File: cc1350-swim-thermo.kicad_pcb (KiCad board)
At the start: 4 copper layers, 60.9 x 60.9 mm, 54 parts, among them P1 LMT_70_1, P2 LMT_70_2, P3 SMA FEMALE, P4 USB_OTG, P5 CONN_02X05, Q1 2N7002, SW1 SW_Push, U1 2450BM14G0011T, U2 XMSSJE3G0PA-003, U3 CC1350F128RSM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

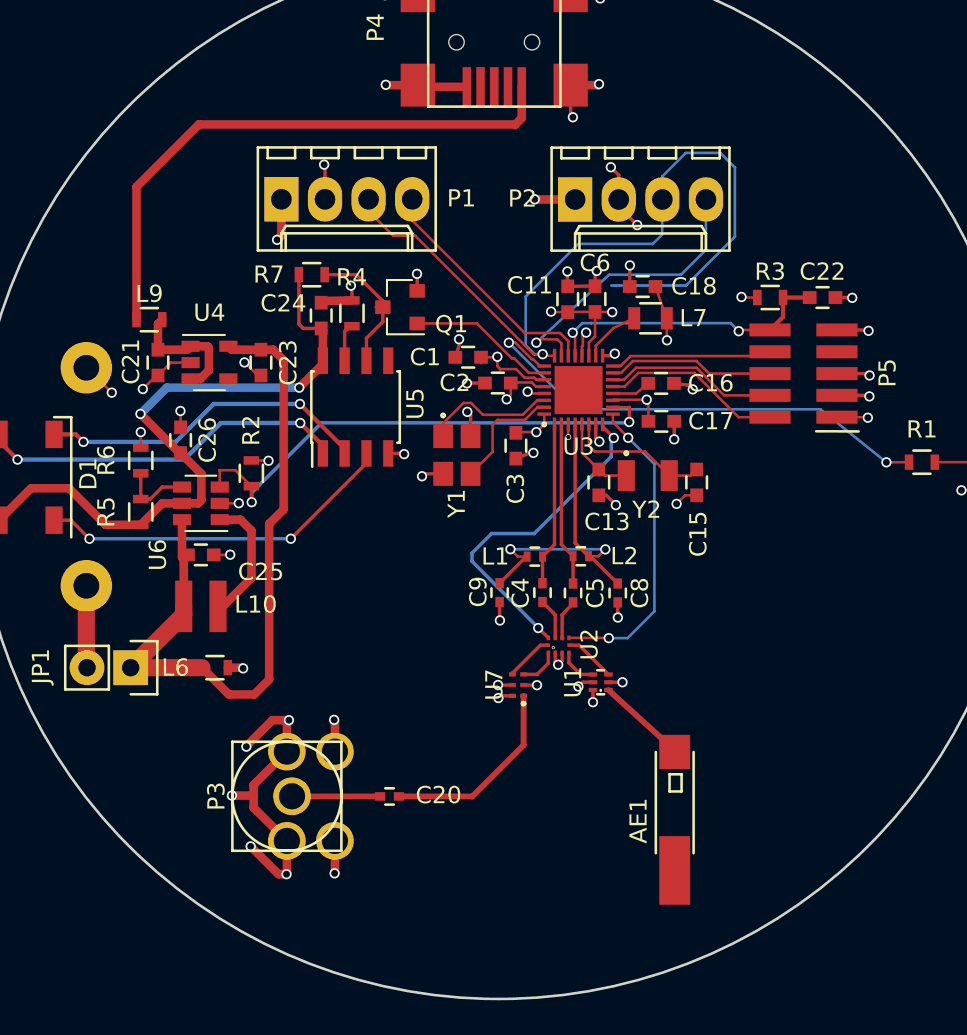
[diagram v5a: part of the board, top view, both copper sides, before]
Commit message: finished wiring, labels and mounting holes
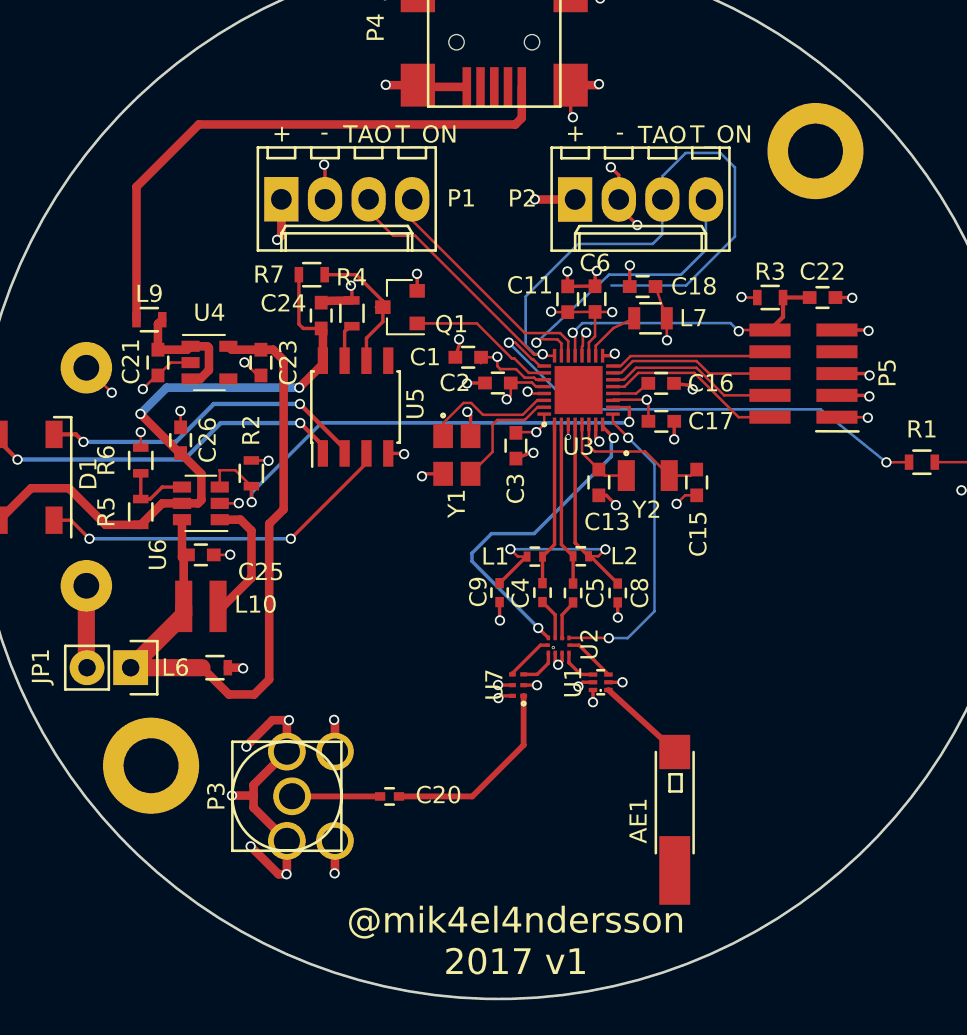
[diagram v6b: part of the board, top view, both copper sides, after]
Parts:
- added REF**: MountingHole_3.2mm_M3_DIN965_Pad, Mounting_Holes:MountingHole_3.2mm_M3_DIN965_Pad, F.Cu at (128.4, 89.3)
- added REF**: MountingHole_3.2mm_M3_DIN965_Pad, Mounting_Holes:MountingHole_3.2mm_M3_DIN965_Pad, F.Cu at (89.7, 125.1)
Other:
- board text added: "+"
- board text added: "-"
- board text added: "@mik4el4ndersson 2017 v1"
- board text added: "Sensor node/concentrator CC1350 sub-GHz and BLE USB or 2xAAA battery"
- board text added: "TAO"
- board text added: "T_ON"

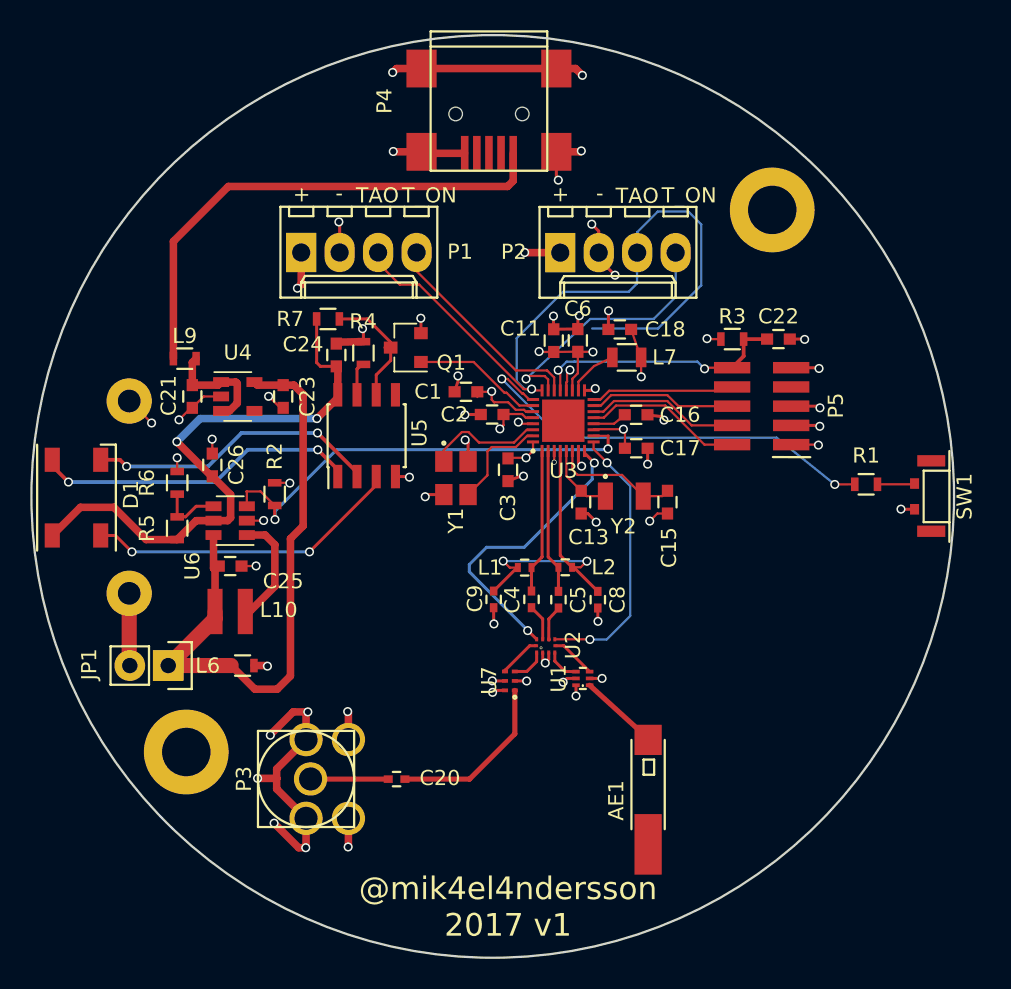
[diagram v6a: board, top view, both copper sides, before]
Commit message: checked first iteration of pcb with real components
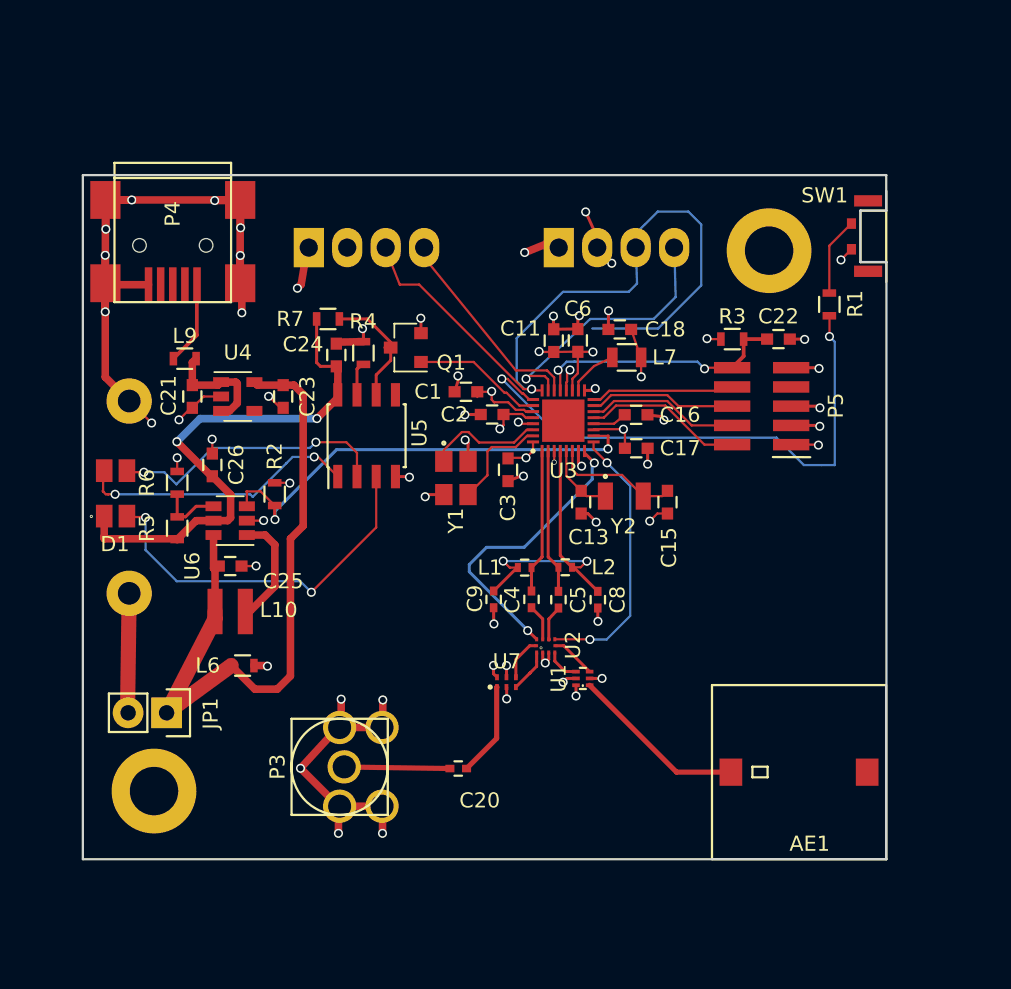
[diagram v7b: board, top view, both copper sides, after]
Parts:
- removed the REF** at (128.4, 89.3)
- removed the REF** at (89.7, 125.1)
- added REF**: MountingHole_3.2mm_M3_DIN965_Pad, Mounting_Holes:MountingHole_3.2mm_M3_DIN965_Pad, F.Cu at (87.6, 127.7)
- added REF**: MountingHole_3.2mm_M3_DIN965_Pad, Mounting_Holes:MountingHole_3.2mm_M3_DIN965_Pad, F.Cu at (128.2, 92.0)
- AE1: footprint cc1350:2450AT42A100 -> cc1350:2450AT45A100
- D1: value CLV1A-FKB -> ASMB-MTB0-0A3A2; footprint LEDs:LED_WS2812B-PLCC4 -> cc1350:ASMB-MTB0-0A3A2
- P1, P2: moved to B.Cu
- moved P4 22.6 mm to (88.8, 90.8)
- moved SW1 17.7 mm to (135.9, 91.0)
- moved R1 12.1 mm to (132.2, 95.5), turned to 90 degrees
- moved AE1 9.18 mm to (124.4, 120.7), turned to 0 degrees
- moved C20 4.13 mm to (107.7, 126.2)
- moved JP1 3.12 mm to (88.4, 122.5)
- moved D1 2.55 mm to (84.3, 106.5), turned to 0 degrees
- moved P3 2.36 mm to (99.8, 126.1)
- moved U7 1.03 mm to (111.5, 120.8), turned to 180 degrees
- moved P1 0.60 mm to (97.8, 91.8)
- moved P2 0.35 mm to (114.3, 91.8)
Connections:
- U5 pad 1: Net-(D1-Pad4) -> Net-(D1-Pad2)
- U5 pad 3: Net-(D1-Pad2) -> Net-(D1-Pad4)
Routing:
- net GND: track 312.9 -> 367.9 mm
- net Net-(L9-Pad2): track 33.7 -> 5.53 mm
- net /SWITCH: track 28.6 -> 37.0 mm
- net Net-(AE1-Pad1): track 5.36 -> 11.7 mm
- net Net-(C20-Pad2): track 11.4 -> 6.21 mm
- net Net-(D1-Pad4): track 21.6 -> 25.5 mm
- net VCC: track 41.5 -> 45.3 mm
- net +5V: track 38.8 -> 35.2 mm
- net Net-(BT1-Pad1): track 4.79 -> 7.91 mm
- net Net-(R1-Pad2): track 2.47 -> 5.19 mm
- net Net-(C20-Pad1): track 5.13 -> 6.98 mm
- net Net-(D1-Pad2): track 21.0 -> 19.2 mm
- net /VDDS: track 110.5 -> 111.5 mm
- net /T_ON_2: track 17.3 -> 18.2 mm
- net /TAO: track 49.4 -> 50.0 mm
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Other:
- board size 60.9 x 60.9 mm -> 53.1 x 45.2 mm
- rule pad_to_mask_clearance: 0.2 -> 0.0762
- board text added: "Sensor node/concentrator CC1350 sub-GHz and BLE USB or 2xAAA battery @mik4el4ndersson v1 2017"
- board text removed: "@mik4el4ndersson 2017 v1"
- board text removed: "Sensor node/concentrator CC1350 sub-GHz and BLE USB or 2xAAA battery"

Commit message: zones and vias
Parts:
- added REF**: VIA_0.34, cc1350:VIA_0.34, F.Cu at (115.5, 104.2)
- added REF**: VIA-0.6mm, cc1350:VIA-0.6mm, F.Cu at (102.8, 103.6)
- added REF**: VIA-0.6mm, cc1350:VIA-0.6mm, F.Cu at (109.5, 93.0)
- added REF**: VIA-0.6mm, cc1350:VIA-0.6mm, F.Cu at (107.6, 119.7)
- added REF**: VIA-0.6mm, cc1350:VIA-0.6mm, F.Cu at (101.5, 114.8)
- added REF**: VIA-0.6mm, cc1350:VIA-0.6mm, F.Cu at (107.2, 115.1)
- added REF**: VIA-0.6mm, cc1350:VIA-0.6mm, F.Cu at (111.5, 110.2)
- added REF**: VIA-0.6mm, cc1350:VIA-0.6mm, F.Cu at (119.2, 117.7)
- added REF**: VIA-0.6mm, cc1350:VIA-0.6mm, F.Cu at (120.2, 115.1)
- added REF**: VIA-0.6mm, cc1350:VIA-0.6mm, F.Cu at (120.1, 111.7)
- added REF**: VIA-0.6mm, cc1350:VIA-0.6mm, F.Cu at (124.4, 114.3)
- added REF**: VIA_0.34, cc1350:VIA_0.34, F.Cu at (114.5, 104.2)
- added REF**: VIA-0.6mm, cc1350:VIA-0.6mm, F.Cu at (124.5, 109.3)
- added REF**: VIA-0.6mm, cc1350:VIA-0.6mm, F.Cu at (130.6, 107.5)
- added REF**: VIA-0.6mm, cc1350:VIA-0.6mm, F.Cu at (130.6, 114.7)
- added REF**: VIA-0.6mm, cc1350:VIA-0.6mm, F.Cu at (125.1, 94.7)
- added REF**: VIA-0.6mm, cc1350:VIA-0.6mm, F.Cu at (135.2, 95.2)
- added REF**: VIA-0.6mm, cc1350:VIA-0.6mm, F.Cu at (135.2, 100.6)
- added REF**: VIA-0.6mm, cc1350:VIA-0.6mm, F.Cu at (135.3, 105.3)
- added REF**: VIA-0.6mm, cc1350:VIA-0.6mm, F.Cu at (135.3, 110.4)
- added REF**: VIA-0.6mm, cc1350:VIA-0.6mm, F.Cu at (135.3, 114.8)
- added REF**: VIA-0.6mm, cc1350:VIA-0.6mm, F.Cu at (135.2, 119.6)
- added REF**: VIA_0.34, cc1350:VIA_0.34, F.Cu at (113.5, 104.2)
- added REF**: VIA-0.6mm, cc1350:VIA-0.6mm, F.Cu at (130.4, 119.6)
- added REF**: VIA-0.6mm, cc1350:VIA-0.6mm, F.Cu at (125.8, 119.6)
- added REF**: VIA-0.6mm, cc1350:VIA-0.6mm, F.Cu at (114.7, 126.6)
- added REF**: VIA-0.6mm, cc1350:VIA-0.6mm, F.Cu at (109.2, 121.9)
- added REF**: VIA-0.6mm, cc1350:VIA-0.6mm, F.Cu at (108.8, 124.0)
- added REF**: VIA-0.6mm, cc1350:VIA-0.6mm, F.Cu at (104.5, 125.1)
- added REF**: VIA-0.6mm, cc1350:VIA-0.6mm, F.Cu at (105.7, 127.2)
- added REF**: VIA-0.6mm, cc1350:VIA-0.6mm, F.Cu at (109.9, 126.1)
- added REF**: VIA-0.6mm, cc1350:VIA-0.6mm, F.Cu at (111.4, 124.3)
- added REF**: VIA-0.6mm, cc1350:VIA-0.6mm, F.Cu at (119.2, 121.7)
- added REF**: VIA_0.34, cc1350:VIA_0.34, F.Cu at (115.5, 103.2)
- added REF**: VIA-0.6mm, cc1350:VIA-0.6mm, F.Cu at (118.0, 124.2)
- added REF**: VIA-0.6mm, cc1350:VIA-0.6mm, F.Cu at (121.0, 126.7)
- added REF**: VIA-0.6mm, cc1350:VIA-0.6mm, F.Cu at (121.5, 124.3)
- added REF**: VIA-0.6mm, cc1350:VIA-0.6mm, F.Cu at (123.6, 121.2)
- added REF**: VIA-0.6mm, cc1350:VIA-0.6mm, F.Cu at (123.6, 124.4)
- added REF**: VIA-0.6mm, cc1350:VIA-0.6mm, F.Cu at (123.6, 129.5)
- added REF**: VIA-0.6mm, cc1350:VIA-0.6mm, F.Cu at (117.6, 129.6)
- added REF**: VIA-0.6mm, cc1350:VIA-0.6mm, F.Cu at (110.1, 131.3)
- added REF**: VIA-0.6mm, cc1350:VIA-0.6mm, F.Cu at (103.8, 131.4)
- added REF**: VIA-0.6mm, cc1350:VIA-0.6mm, F.Cu at (99.4, 110.5)
- added REF**: VIA_0.34, cc1350:VIA_0.34, F.Cu at (114.5, 103.2)
- added REF**: VIA-0.6mm, cc1350:VIA-0.6mm, F.Cu at (104.8, 112.1)
- added REF**: VIA-0.6mm, cc1350:VIA-0.6mm, F.Cu at (105.3, 118.1)
- added REF**: VIA-0.6mm, cc1350:VIA-0.6mm, F.Cu at (98.8, 119.0)
- added REF**: VIA-0.6mm, cc1350:VIA-0.6mm, F.Cu at (93.3, 122.7)
- added REF**: VIA-0.6mm, cc1350:VIA-0.6mm, F.Cu at (93.2, 126.9)
- added REF**: VIA-0.6mm, cc1350:VIA-0.6mm, F.Cu at (97.4, 131.4)
- added REF**: VIA-0.6mm, cc1350:VIA-0.6mm, F.Cu at (91.2, 131.4)
- added REF**: VIA-0.6mm, cc1350:VIA-0.6mm, F.Cu at (83.7, 131.4)
- added REF**: VIA-0.6mm, cc1350:VIA-0.6mm, F.Cu at (83.6, 125.9)
- added REF**: VIA-0.6mm, cc1350:VIA-0.6mm, F.Cu at (83.6, 117.8)
- added REF**: VIA_0.34, cc1350:VIA_0.34, F.Cu at (113.5, 103.2)
- added REF**: VIA-0.6mm, cc1350:VIA-0.6mm, F.Cu at (83.6, 111.7)
- added REF**: VIA-0.6mm, cc1350:VIA-0.6mm, F.Cu at (83.5, 104.1)
- added REF**: VIA-0.6mm, cc1350:VIA-0.6mm, F.Cu at (83.6, 97.5)
- added REF**: VIA-0.6mm, cc1350:VIA-0.6mm, F.Cu at (96.3, 87.7)
- added REF**: VIA-0.6mm, cc1350:VIA-0.6mm, F.Cu at (101.7, 89.3)
- added REF**: VIA-0.6mm, cc1350:VIA-0.6mm, F.Cu at (108.3, 87.7)
- added REF**: VIA-0.6mm, cc1350:VIA-0.6mm, F.Cu at (112.8, 87.7)
- added REF**: VIA-0.6mm, cc1350:VIA-0.6mm, F.Cu at (118.4, 89.3)
- added REF**: VIA-0.6mm, cc1350:VIA-0.6mm, F.Cu at (124.8, 87.7)
- added REF**: VIA-0.6mm, cc1350:VIA-0.6mm, F.Cu at (129.7, 87.7)
- added REF**: VIA_0.34, cc1350:VIA_0.34, F.Cu at (115.5, 102.2)
- added REF**: VIA-0.6mm, cc1350:VIA-0.6mm, F.Cu at (135.1, 87.7)
- added REF**: VIA_0.34, cc1350:VIA_0.34, F.Cu at (113.5, 102.2)
- added REF**: VIA_0.34, cc1350:VIA_0.34, F.Cu at (114.5, 102.2)
- added REF**: VIA-0.6mm, cc1350:VIA-0.6mm, F.Cu at (127.9, 111.4)
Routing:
- net /TAO: track 50.0 -> 31.8 mm
- net GND: track 367.9 -> 370.1 mm, vias 57 -> 58
- net /T_ON_1: track 14.4 -> 15.4 mm
- net /VDDR: track 22.5 -> 23.2 mm
- added copper zone on In2.Cu, net /VDDS
- added copper zone on B.Cu, net GND
- added copper zone on F.Cu, net GND
- added copper zone on In1.Cu, net GND
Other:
- net class 50ohm added: clearance 0.34, trace_width 0.34, via_dia 0.6, via_drill 0.4
